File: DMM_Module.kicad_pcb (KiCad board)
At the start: 4 copper layers, 60 x 96 mm, 123 parts, among them J1 M20-7810245, J2 M20-7810245, J3 M20-7812045, J4 M20-7812045, J5 M20-7810245, J6 M20-7810245, K1 G6K-2F-Y-TR, K2 G6K-2F-Y-TR, K3 G6K-2F-Y-TR, K4 G6K-2F-Y-TR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

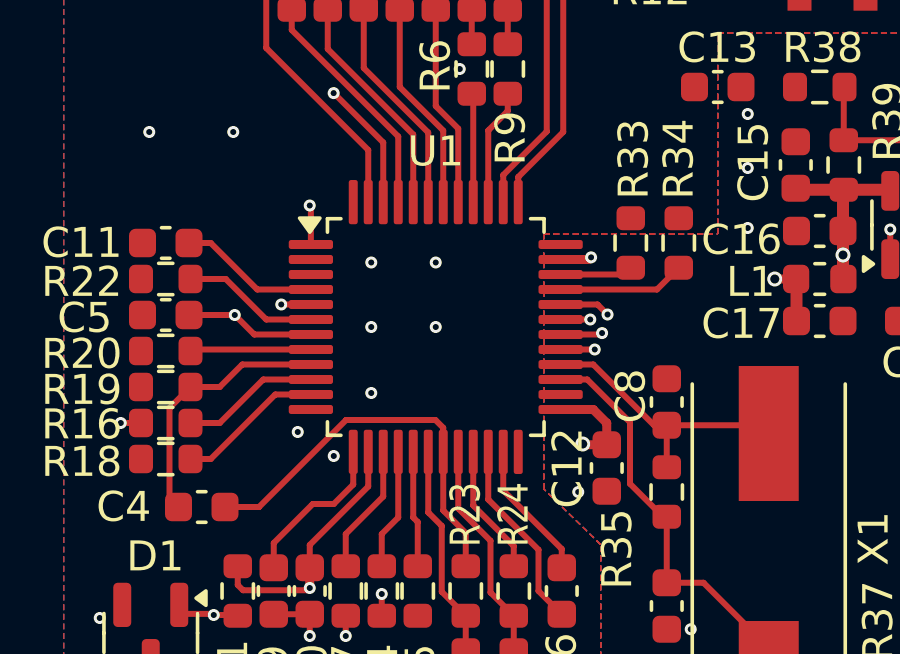
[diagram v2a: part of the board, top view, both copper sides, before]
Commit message: U1 pad thickness was reduced to 0.28 to comply with the manufacturer's constraints
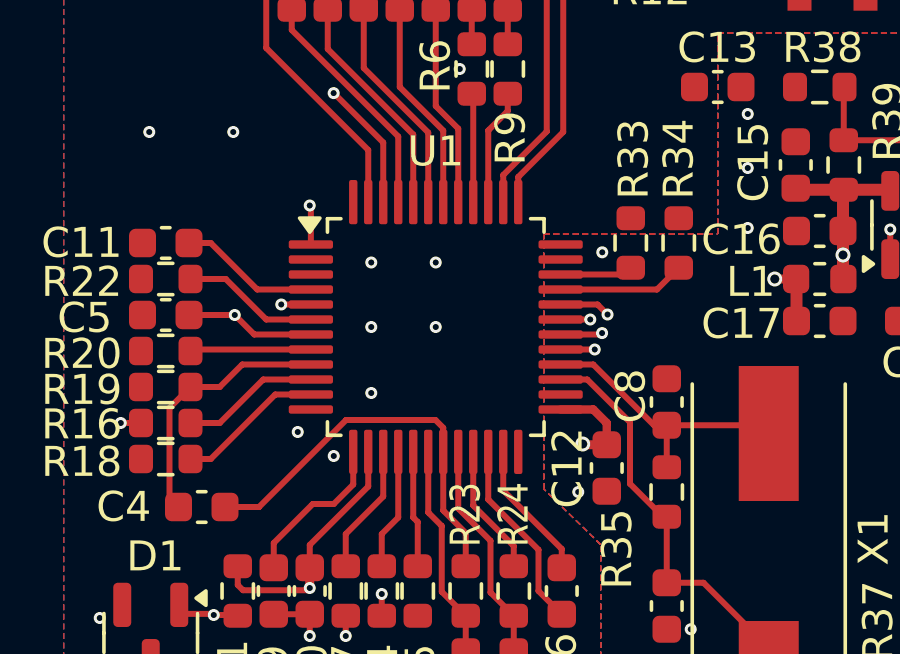
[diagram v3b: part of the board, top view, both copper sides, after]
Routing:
- net VSSA: track 20.6 -> 19.5 mm
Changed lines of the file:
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@@
 		(pad "1" smd roundrect
 			(at -4.1625 -2.75)
-			(size 1.475 0.3)
+			(size 1.475 0.28)
 			(layers "F.Cu" "F.Paste" "F.Mask")
 			(roundrect_rratio 0.25)
@@
 		(pad "2" smd roundrect
 			(at -4.1625 -2.25)
-			(size 1.475 0.3)
+			(size 1.475 0.28)
 			(layers "F.Cu" "F.Paste" "F.Mask")
 			(roundrect_rratio 0.25)
@@
 		(pad "3" smd roundrect
 			(at -4.1625 -1.75)
-			(size 1.475 0.3)
+			(size 1.475 0.28)
 			(layers "F.Cu" "F.Paste" "F.Mask")
 			(roundrect_rratio 0.25)
@@
 		(pad "4" smd roundrect
 			(at -4.1625 -1.25)
-			(size 1.475 0.3)
+			(size 1.475 0.28)
 			(layers "F.Cu" "F.Paste" "F.Mask")
 			(roundrect_rratio 0.25)
@@
 		(pad "5" smd roundrect
 			(at -4.1625 -0.75)
-			(size 1.475 0.3)
+			(size 1.475 0.28)
 			(layers "F.Cu" "F.Paste" "F.Mask")
 			(roundrect_rratio 0.25)
@@
 		(pad "6" smd roundrect
 			(at -4.1625 -0.25)
-			(size 1.475 0.3)
+			(size 1.475 0.28)
 			(layers "F.Cu" "F.Paste" "F.Mask")
 			(roundrect_rratio 0.25)
@@
 		(pad "7" smd roundrect
 			(at -4.1625 0.25)
-			(size 1.475 0.3)
+			(size 1.475 0.28)
 			(layers "F.Cu" "F.Paste" "F.Mask")
 			(roundrect_rratio 0.25)
@@
 		(pad "8" smd roundrect
 			(at -4.1625 0.75)
-			(size 1.475 0.3)
+			(size 1.475 0.28)
 			(layers "F.Cu" "F.Paste" "F.Mask")
 			(roundrect_rratio 0.25)
@@
 		(pad "9" smd roundrect
 			(at -4.1625 1.25)
-			(size 1.475 0.3)
+			(size 1.475 0.28)
 			(layers "F.Cu" "F.Paste" "F.Mask")
 			(roundrect_rratio 0.25)
@@
 		(pad "10" smd roundrect
 			(at -4.1625 1.75)
-			(size 1.475 0.3)
+			(size 1.475 0.28)
 			(layers "F.Cu" "F.Paste" "F.Mask")
 			(roundrect_rratio 0.25)
@@
 		(pad "11" smd roundrect
 			(at -4.1625 2.25)
-			(size 1.475 0.3)
+			(size 1.475 0.28)
 			(layers "F.Cu" "F.Paste" "F.Mask")
 			(roundrect_rratio 0.25)
@@
 		(pad "12" smd roundrect
 			(at -4.1625 2.75)
-			(size 1.475 0.3)
+			(size 1.475 0.28)
 			(layers "F.Cu" "F.Paste" "F.Mask")
 			(roundrect_rratio 0.25)
@@
 		(pad "13" smd roundrect
 			(at -2.75 4.1625)
-			(size 0.3 1.475)
+			(size 0.28 1.475)
 			(layers "F.Cu" "F.Paste" "F.Mask")
 			(roundrect_rratio 0.25)
@@
 		(pad "14" smd roundrect
 			(at -2.25 4.1625)
-			(size 0.3 1.475)
+			(size 0.28 1.475)
 			(layers "F.Cu" "F.Paste" "F.Mask")
 			(roundrect_rratio 0.25)
@@
 		(pad "15" smd roundrect
 			(at -1.75 4.1625)
-			(size 0.3 1.475)
+			(size 0.28 1.475)
 			(layers "F.Cu" "F.Paste" "F.Mask")
 			(roundrect_rratio 0.25)
@@
 		(pad "16" smd roundrect
 			(at -1.25 4.1625)
-			(size 0.3 1.475)
+			(size 0.28 1.475)
 			(layers "F.Cu" "F.Paste" "F.Mask")
 			(roundrect_rratio 0.25)
@@
 		(pad "17" smd roundrect
 			(at -0.75 4.1625)
-			(size 0.3 1.475)
+			(size 0.28 1.475)
 			(layers "F.Cu" "F.Paste" "F.Mask")
 			(roundrect_rratio 0.25)
@@
 		(pad "18" smd roundrect
 			(at -0.25 4.1625)
-			(size 0.3 1.475)
+			(size 0.28 1.475)
 			(layers "F.Cu" "F.Paste" "F.Mask")
 			(roundrect_rratio 0.25)
@@
 		(pad "19" smd roundrect
 			(at 0.25 4.1625)
-			(size 0.3 1.475)
+			(size 0.28 1.475)
 			(layers "F.Cu" "F.Paste" "F.Mask")
 			(roundrect_rratio 0.25)
@@
 		(pad "20" smd roundrect
 			(at 0.75 4.1625)
-			(size 0.3 1.475)
+			(size 0.28 1.475)
 			(layers "F.Cu" "F.Paste" "F.Mask")
 			(roundrect_rratio 0.25)
@@
 		(pad "21" smd roundrect
 			(at 1.25 4.1625)
-			(size 0.3 1.475)
+			(size 0.28 1.475)
 			(layers "F.Cu" "F.Paste" "F.Mask")
 			(roundrect_rratio 0.25)
@@
 		(pad "22" smd roundrect
 			(at 1.75 4.1625)
-			(size 0.3 1.475)
+			(size 0.28 1.475)
 			(layers "F.Cu" "F.Paste" "F.Mask")
 			(roundrect_rratio 0.25)
@@
 		(pad "23" smd roundrect
 			(at 2.25 4.1625)
-			(size 0.3 1.475)
+			(size 0.28 1.475)
 			(layers "F.Cu" "F.Paste" "F.Mask")
 			(roundrect_rratio 0.25)
@@
 		(pad "24" smd roundrect
 			(at 2.75 4.1625)
-			(size 0.3 1.475)
+			(size 0.28 1.475)
 			(layers "F.Cu" "F.Paste" "F.Mask")
 			(roundrect_rratio 0.25)
@@
 		(pad "25" smd roundrect
 			(at 4.1625 2.75)
-			(size 1.475 0.3)
+			(size 1.475 0.28)
 			(layers "F.Cu" "F.Paste" "F.Mask")
 			(roundrect_rratio 0.25)
@@
 		(pad "26" smd roundrect
 			(at 4.1625 2.25)
-			(size 1.475 0.3)
+			(size 1.475 0.28)
 			(layers "F.Cu" "F.Paste" "F.Mask")
 			(roundrect_rratio 0.25)
@@
 		(pad "27" smd roundrect
 			(at 4.1625 1.75)
-			(size 1.475 0.3)
+			(size 1.475 0.28)
 			(layers "F.Cu" "F.Paste" "F.Mask")
 			(roundrect_rratio 0.25)
@@
 		(pad "28" smd roundrect
 			(at 4.1625 1.25)
-			(size 1.475 0.3)
+			(size 1.475 0.28)
 			(layers "F.Cu" "F.Paste" "F.Mask")
 			(roundrect_rratio 0.25)
@@
 		(pad "29" smd roundrect
 			(at 4.1625 0.75)
-			(size 1.475 0.3)
+			(size 1.475 0.28)
 			(layers "F.Cu" "F.Paste" "F.Mask")
 			(roundrect_rratio 0.25)
@@
 		(pad "30" smd roundrect
 			(at 4.1625 0.25)
-			(size 1.475 0.3)
+			(size 1.475 0.28)
 			(layers "F.Cu" "F.Paste" "F.Mask")
 			(roundrect_rratio 0.25)
@@
 		(pad "31" smd roundrect
 			(at 4.1625 -0.25)
-			(size 1.475 0.3)
+			(size 1.475 0.28)
 			(layers "F.Cu" "F.Paste" "F.Mask")
 			(roundrect_rratio 0.25)
@@
 		(pad "32" smd roundrect
 			(at 4.1625 -0.75)
-			(size 1.475 0.3)
+			(size 1.475 0.28)
 			(layers "F.Cu" "F.Paste" "F.Mask")
 			(roundrect_rratio 0.25)
@@
 		(pad "33" smd roundrect
 			(at 4.1625 -1.25)
-			(size 1.475 0.3)
+			(size 1.475 0.28)
 			(layers "F.Cu" "F.Paste" "F.Mask")
 			(roundrect_rratio 0.25)
@@
 		(pad "34" smd roundrect
 			(at 4.1625 -1.75)
-			(size 1.475 0.3)
+			(size 1.475 0.28)
 			(layers "F.Cu" "F.Paste" "F.Mask")
 			(roundrect_rratio 0.25)
@@
 		(pad "35" smd roundrect
 			(at 4.1625 -2.25)
-			(size 1.475 0.3)
+			(size 1.475 0.28)
 			(layers "F.Cu" "F.Paste" "F.Mask")
 			(roundrect_rratio 0.25)
@@
 		(pad "36" smd roundrect
 			(at 4.1625 -2.75)
-			(size 1.475 0.3)
+			(size 1.475 0.28)
 			(layers "F.Cu" "F.Paste" "F.Mask")
 			(roundrect_rratio 0.25)
@@
 		(pad "37" smd roundrect
 			(at 2.75 -4.1625)
-			(size 0.3 1.475)
+			(size 0.28 1.475)
 			(layers "F.Cu" "F.Paste" "F.Mask")
 			(roundrect_rratio 0.25)
@@
 		(pad "38" smd roundrect
 			(at 2.25 -4.1625)
-			(size 0.3 1.475)
+			(size 0.28 1.475)
 			(layers "F.Cu" "F.Paste" "F.Mask")
 			(roundrect_rratio 0.25)
@@
 		(pad "39" smd roundrect
 			(at 1.75 -4.1625)
-			(size 0.3 1.475)
+			(size 0.28 1.475)
 			(layers "F.Cu" "F.Paste" "F.Mask")
 			(roundrect_rratio 0.25)
@@
 		(pad "40" smd roundrect
 			(at 1.25 -4.1625)
-			(size 0.3 1.475)
+			(size 0.28 1.475)
 			(layers "F.Cu" "F.Paste" "F.Mask")
 			(roundrect_rratio 0.25)
@@
 		(pad "41" smd roundrect
 			(at 0.75 -4.1625)
-			(size 0.3 1.475)
+			(size 0.28 1.475)
 			(layers "F.Cu" "F.Paste" "F.Mask")
 			(roundrect_rratio 0.25)
@@
 		(pad "42" smd roundrect
 			(at 0.25 -4.1625)
-			(size 0.3 1.475)
+			(size 0.28 1.475)
 			(layers "F.Cu" "F.Paste" "F.Mask")
 			(roundrect_rratio 0.25)
@@
 		(pad "43" smd roundrect
 			(at -0.25 -4.1625)
-			(size 0.3 1.475)
+			(size 0.28 1.475)
 			(layers "F.Cu" "F.Paste" "F.Mask")
 			(roundrect_rratio 0.25)
@@
 		(pad "44" smd roundrect
 			(at -0.75 -4.1625)
-			(size 0.3 1.475)
+			(size 0.28 1.475)
 			(layers "F.Cu" "F.Paste" "F.Mask")
 			(roundrect_rratio 0.25)
@@
 		(pad "45" smd roundrect
 			(at -1.25 -4.1625)
-			(size 0.3 1.475)
+			(size 0.28 1.475)
 			(layers "F.Cu" "F.Paste" "F.Mask")
 			(roundrect_rratio 0.25)
@@
 		(pad "46" smd roundrect
 			(at -1.75 -4.1625)
-			(size 0.3 1.475)
+			(size 0.28 1.475)
 			(layers "F.Cu" "F.Paste" "F.Mask")
 			(roundrect_rratio 0.25)
@@
 		(pad "47" smd roundrect
 			(at -2.25 -4.1625)
-			(size 0.3 1.475)
+			(size 0.28 1.475)
 			(layers "F.Cu" "F.Paste" "F.Mask")
 			(roundrect_rratio 0.25)
@@
 		(pad "48" smd roundrect
 			(at -2.75 -4.1625)
-			(size 0.3 1.475)
+			(size 0.28 1.475)
 			(layers "F.Cu" "F.Paste" "F.Mask")
 			(roundrect_rratio 0.25)
@@
 	)
 	(segment
-		(start 168.473602 86.668602)
-		(end 168.402204 86.74)
-		(width 0.3)
-		(layer "F.Cu")
-		(net 18)
-	)
-	(segment
 		(start 159.132 88.2395)
 		(end 159.1325 88.24)
@@
 	)
 	(segment
-		(start 168.402204 86.74)
-		(end 167.4575 86.74)
-		(width 0.3)
-		(layer "F.Cu")
-		(net 18)
-	)
-	(segment
 		(start 168.995 94.465)
 		(end 168.895 94.565)
@@
 	)
 	(via
-		(at 168.473602 86.668602)
+		(at 168.845 86.5)
 		(size 0.4)
 		(drill 0.2)
@@
 		(start 168.545 91.74)
 		(end 168.995 92.19)
-		(width 0.3)
+		(width 0.28)
 		(layer "F.Cu")
 		(net 22)
@@
 		(start 167.4575 91.74)
 		(end 168.545 91.74)
-		(width 0.3)
+		(width 0.28)
 		(layer "F.Cu")
 		(net 22)
@@
 		(start 168.995 92.19)
 		(end 168.995 92.915)
-		(width 0.3)
+		(width 0.28)
 		(layer "F.Cu")
 		(net 22)
